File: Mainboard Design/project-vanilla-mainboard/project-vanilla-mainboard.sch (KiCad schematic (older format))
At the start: 5 parts

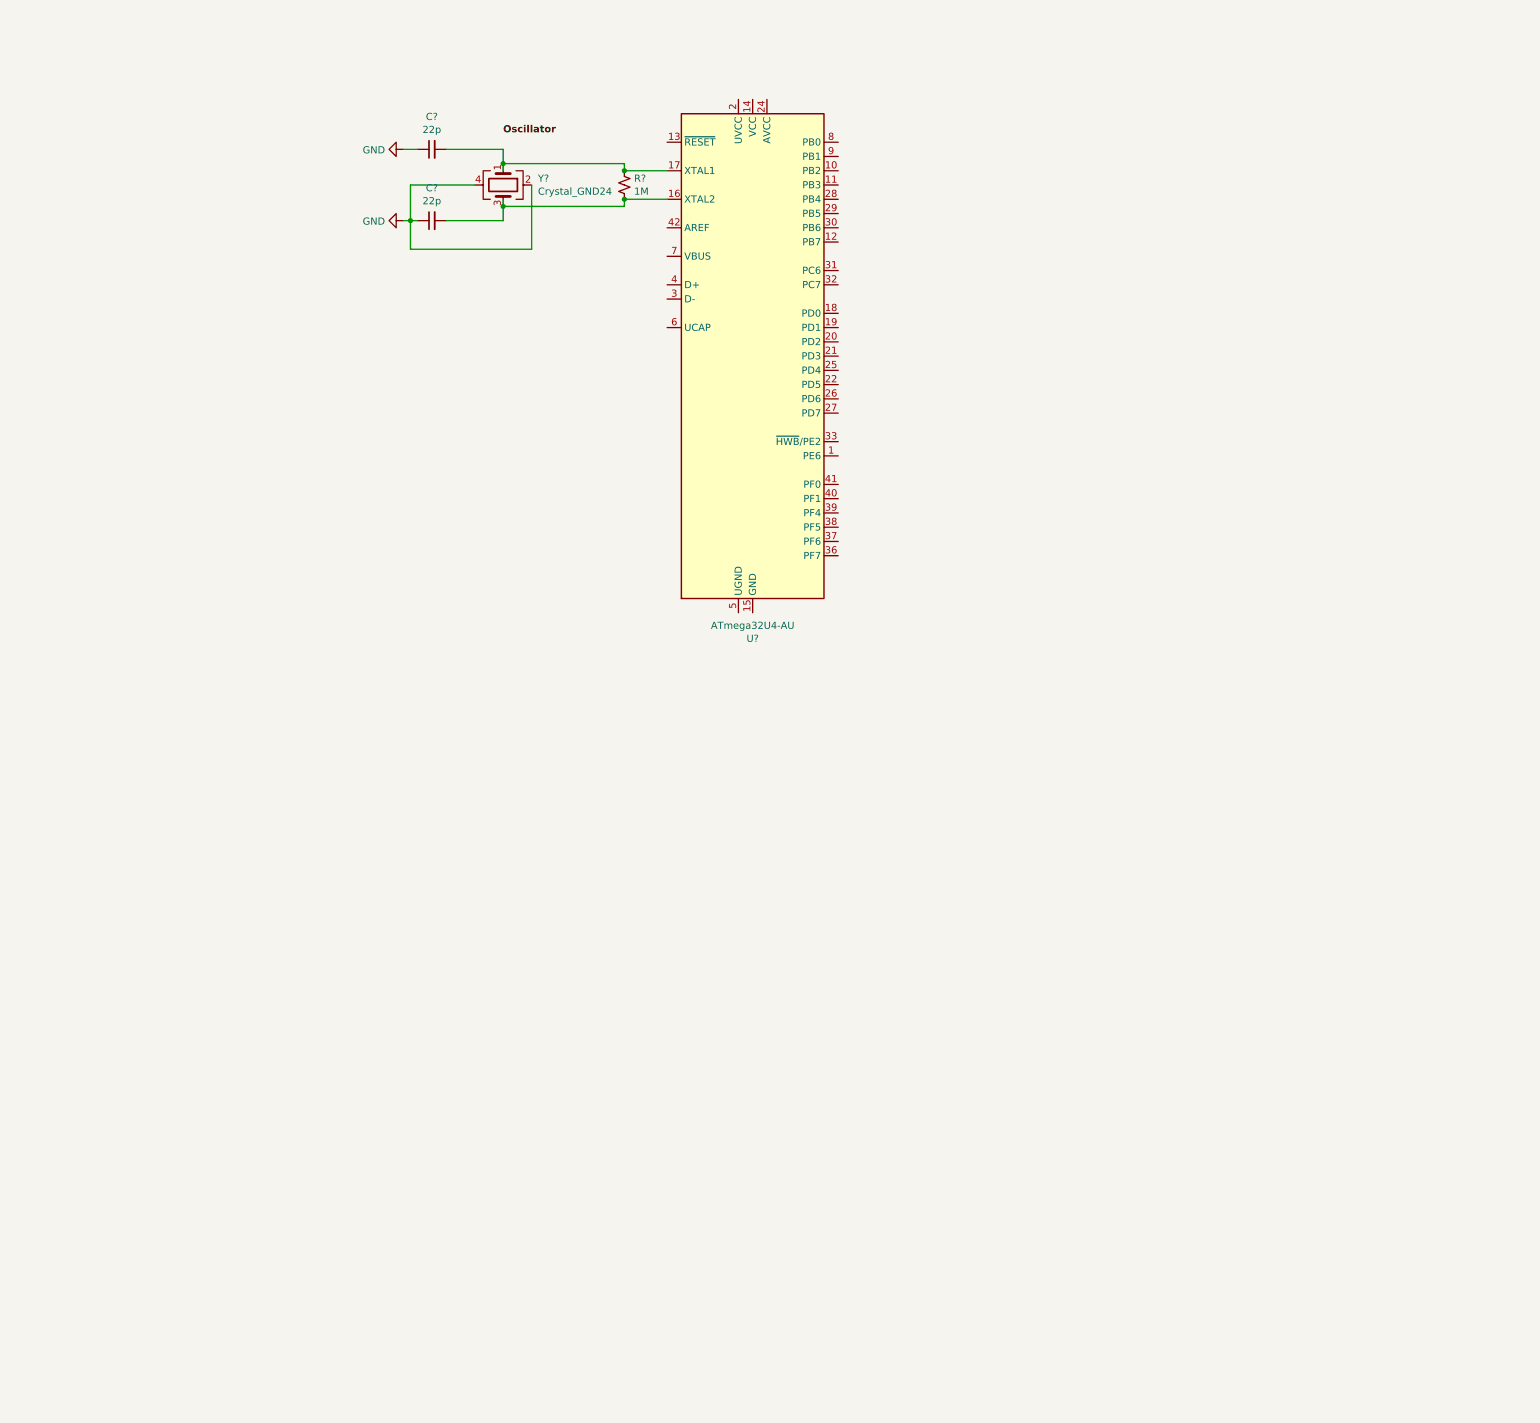
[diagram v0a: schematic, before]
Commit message: Major changes to both case design and mainboard schematic. Nothing final yet.
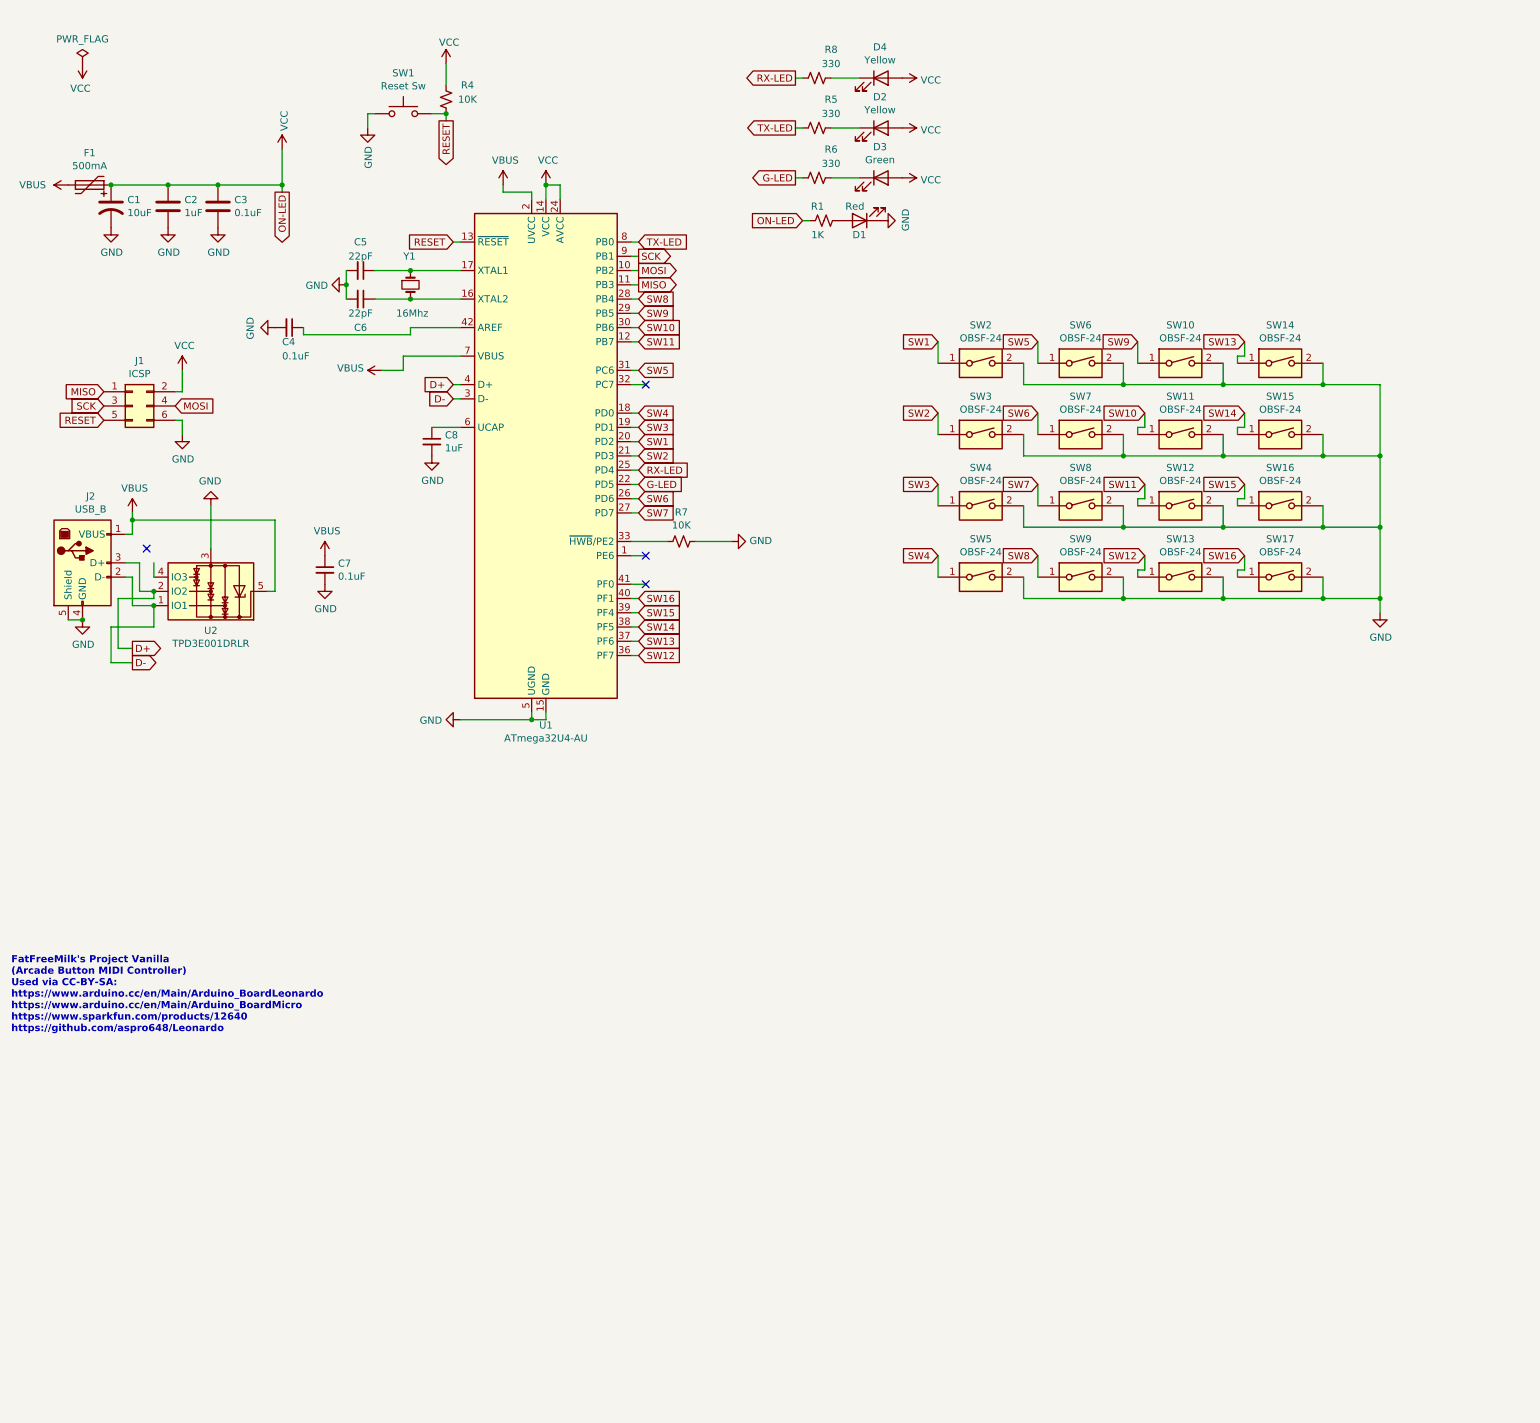
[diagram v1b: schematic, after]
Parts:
- removed C? (x2): 22p, symbol Device:C_Small
- removed R?: 1M, symbol Device:R_Small_US
- removed U?: ATmega32U4-AU, Package_QFP:TQFP-44_10x10mm_P0.8mm, symbol MCU_Microchip_ATmega:ATmega32U4-AU
- removed Y?: Crystal_GND24, symbol Device:Crystal_GND24
- added C1: 10uF, symbol Device:CP1
- added C2: 1uF, symbol Device:C
- added C3: 0.1uF, symbol Device:C
- added C4, C7: 0.1uF, symbol Device:C_Small
- added C5, C6: 22pF, symbol Device:C_Small
- added C8: 1uF, symbol Device:C_Small
- added D1: Red, symbol Device:LED
- added D2, D4: Yellow, symbol Device:LED
- added D3: Green, symbol Device:LED
- added F1: 500mA, symbol Device:Polyfuse
- added J1: ICSP, symbol Connector_Generic:Conn_02x03_Odd_Even
- added J2: USB_B, symbol Connector:USB_B
- added R1: 1K, symbol Device:R_Small_US
- added R4, R7: 10K, symbol Device:R_Small_US
- added R5, R6, R8: 330, symbol Device:R_Small_US
- added SW1: Reset Sw, symbol Switch:SW_MEC_5G
- added SW10, SW11, SW12, SW13, SW14, SW15, SW16, SW17, SW2, SW3, SW4, SW5, SW6, SW7, SW8, SW9: OBSF-24, symbol Switch:SW_DIP_x01
- added U1: ATmega32U4-AU, Package_QFP:TQFP-44_10x10mm_P0.8mm, symbol MCU_Microchip_ATmega:ATmega32U4-AU
- added U2: TPD3E001DRLR, Package_TO_SOT_SMD:SOT-553, symbol Power_Protection:TPD3E001DRLR
- added Y1: 16Mhz, symbol Device:Crystal_Small
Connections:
- net labels added: D+, D-, G-LED, MISO, MOSI, ON-LED, RESET, RX-LED, SCK, SW1, SW10, SW11, SW12, SW13, SW14, SW15, SW16, SW2, SW3, SW4, SW5, SW6, SW7, SW8, SW9, TX-LED, VBUS, VCC
- net labels removed: Oscillator
- wire segments 20 -> 164
- no-connect marks 0 -> 4
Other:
- note added: "FatFreeMilk's Project Vanilla\n(Arcade Button MIDI Controller)\nUsed via CC-BY-SA:\nhttps://www.arduino.cc/en/Main/Arduino_BoardLeonardo\nhttps://www.arduino.cc/en/Main/Arduino_BoardMicro\nhttps://www.sparkfun.com/products/12640\nhttps://github.com/aspro648/Leonardo"

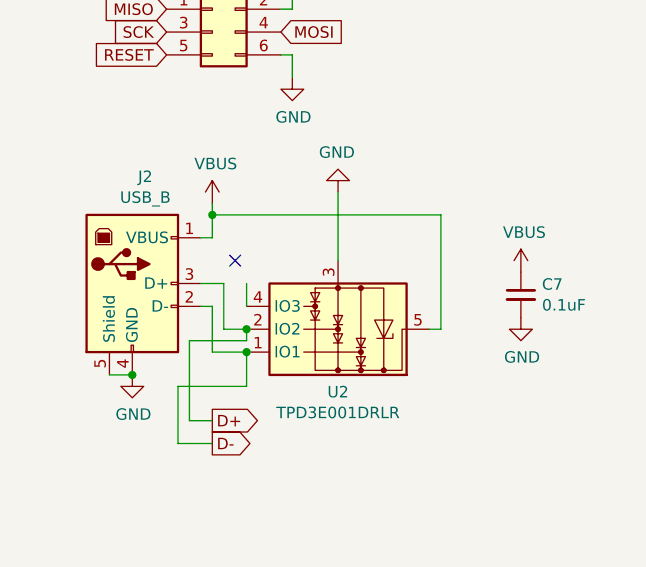
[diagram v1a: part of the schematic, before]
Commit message: Started work on the case in FreeCAD (new design).
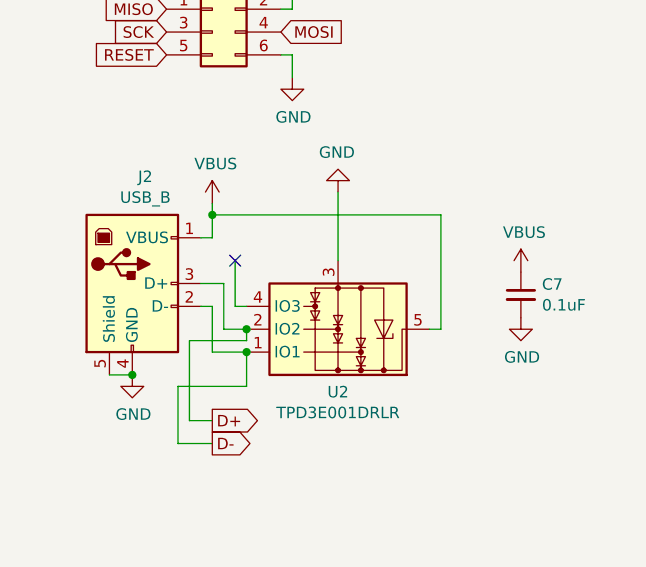
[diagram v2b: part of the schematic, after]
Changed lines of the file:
@@
 Wire Wire Line
 	1950 4000 1950 4300
-NoConn ~ 1500 4300
-Wire Wire Line
-	1550 4400 1550 4500
 Wire Wire Line
 	3600 1250 3600 1300
@@
 Wire Wire Line
 	3650 2150 3700 2150
+NoConn ~ 1500 4300
+Wire Wire Line
+	1550 4500 1500 4500
+Wire Wire Line
+	1500 4500 1500 4300
 $EndSCHEMATC

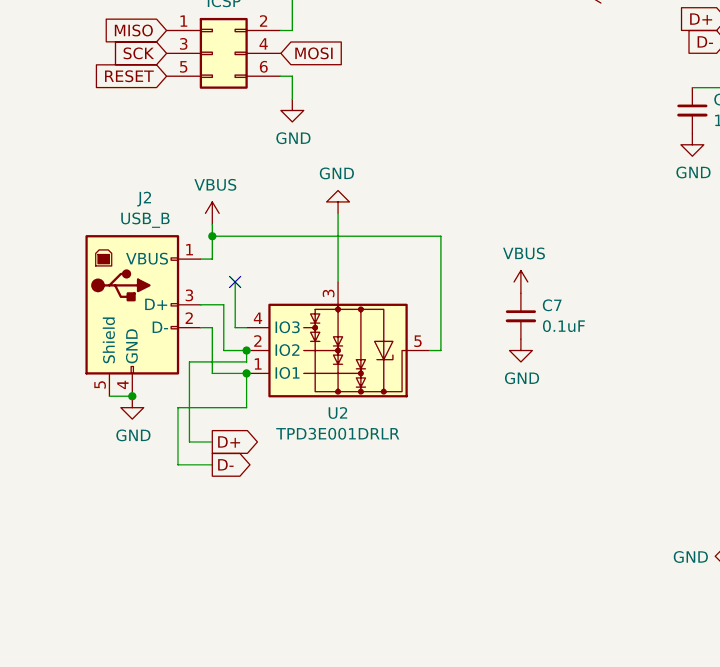
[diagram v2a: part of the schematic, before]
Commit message: In the middle of updating schematic and finishing shell design.
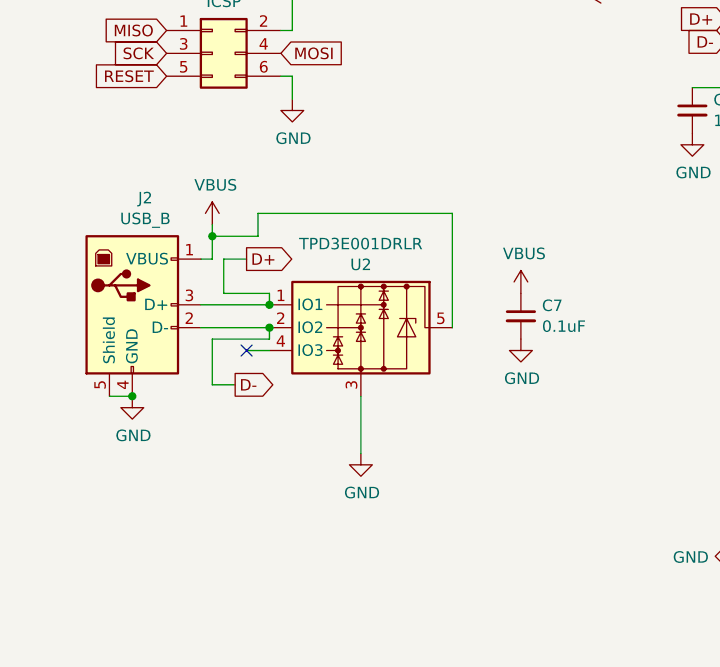
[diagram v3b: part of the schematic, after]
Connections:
- net D+: now also U2.1 (IO1); no longer U2.2 (IO2)
- net D-: now also U2.2 (IO2); no longer U2.1 (IO1)
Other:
- moved on the sheet: U2
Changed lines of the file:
@@
-$EndComp
-$Comp
-L Connector:USB_B J2
-U 1 1 5FF3196E
-P 1050 4400
-F 0 "J2" H 1107 4867 50  0000 C CNN
-F 1 "USB_B" H 1107 4776 50  0000 C CNN
-F 2 "" H 1200 4350 50  0001 C CNN
-F 3 " ~" H 1200 4350 50  0001 C CNN
-	1    1050 4400
-	1    0    0    -1
 $EndComp
 $Comp
@@
 Wire Wire Line
 	950  4800 1050 4800
-Connection ~ 1050 4800
-Wire Wire Line
-	1400 4050 1400 4100
 Wire Wire Line
 	1400 4200 1350 4200
@@
 L Power_Protection:TPD3E001DRLR U2
 U 1 1 60054A8D
-P 1950 4600
-F 0 "U2" H 1950 4875 50  0000 C CNN
-F 1 "TPD3E001DRLR" H 1950 4966 50  0000 C CNN
-F 2 "Package_TO_SOT_SMD:SOT-553" H 1250 4300 50  0001 C CNN
-F 3 "http://www.ti.com/lit/ds/symlink/tpd3e001.pdf" H 1750 4850 50  0001 C CNN
-	1    1950 4600
-	-1   0    0    1
-$EndComp
-Wire Wire Line
-	1400 4100 2400 4100
-Connection ~ 1400 4100
-Wire Wire Line
-	1400 4100 1400 4200
-Wire Wire Line
-	2400 4600 2350 4600
-Wire Wire Line
-	2400 4100 2400 4600
-Wire Wire Line
-	1350 4500 1400 4500
-Wire Wire Line
-	1400 4500 1400 4700
-Wire Wire Line
-	1400 4700 1550 4700
-Wire Wire Line
-	1350 4400 1450 4400
-Wire Wire Line
-	1450 4400 1450 4600
-Wire Wire Line
-	1450 4600 1550 4600
-Text GLabel 1400 5000 2    50   Output ~ 0
-D+
-Text GLabel 1400 5100 2    50   Output ~ 0
-D-
-Wire Wire Line
-	1550 4700 1550 4850
-Wire Wire Line
-	1550 4850 1250 4850
-Wire Wire Line
-	1250 4850 1250 5100
-Wire Wire Line
-	1250 5100 1400 5100
-Connection ~ 1550 4700
-Wire Wire Line
-	1550 4600 1550 4650
-Wire Wire Line
-	1550 4650 1300 4650
-Wire Wire Line
-	1300 4650 1300 5000
-Wire Wire Line
-	1300 5000 1400 5000
-Connection ~ 1550 4600
+P 2050 4500
+F 0 "U2" H 2050 4775 50  0000 C CNN
+F 1 "TPD3E001DRLR" H 2050 4866 50  0000 C CNN
+F 2 "Package_TO_SOT_SMD:SOT-553" H 1350 4200 50  0001 C CNN
+F 3 "http://www.ti.com/lit/ds/symlink/tpd3e001.pdf" H 1850 4750 50  0001 C CNN
+	1    2050 4500
+	-1   0    0    -1
+$EndComp
 Text GLabel 3650 3150 0    50   Input ~ 0
 D+
@@
 L power:GND #PWR0128
 U 1 1 60167591
-P 1950 4000
-F 0 "#PWR0128" H 1950 3750 50  0001 C CNN
-F 1 "GND" H 1955 3827 50  0000 C CNN
-F 2 "" H 1950 4000 50  0001 C CNN
-F 3 "" H 1950 4000 50  0001 C CNN
-	1    1950 4000
-	-1   0    0    1
-$EndComp
-Wire Wire Line
-	1950 4000 1950 4300
+P 2050 5050
+F 0 "#PWR0128" H 2050 4800 50  0001 C CNN
+F 1 "GND" H 2055 4877 50  0000 C CNN
+F 2 "" H 2050 5050 50  0001 C CNN
+F 3 "" H 2050 5050 50  0001 C CNN
+	1    2050 5050
+	1    0    0    -1
+$EndComp
 Wire Wire Line
 	3600 1250 3600 1300
@@
 Wire Wire Line
 	3650 2150 3700 2150
-NoConn ~ 1500 4300
-Wire Wire Line
-	1550 4500 1500 4500
-Wire Wire Line
-	1500 4500 1500 4300
+Connection ~ 1050 4800
+$Comp
+L Connector:USB_B J2
+U 1 1 5FF3196E
+P 1050 4400
+F 0 "J2" H 1107 4867 50  0000 C CNN
+F 1 "USB_B" H 1107 4776 50  0000 C CNN
+F 2 "" H 1200 4350 50  0001 C CNN
+F 3 " ~" H 1200 4350 50  0001 C CNN
+	1    1050 4400
+	1    0    0    -1
+$EndComp
+Wire Wire Line
+	1400 4050 1400 4100
+Wire Wire Line
+	1350 4400 1650 4400
+Wire Wire Line
+	1350 4500 1650 4500
+Wire Wire Line
+	1650 4600 1550 4600
+NoConn ~ 1550 4600
+Wire Wire Line
+	1400 4100 1600 4100
+Wire Wire Line
+	1600 4100 1600 4000
+Wire Wire Line
+	1600 4000 2450 4000
+Wire Wire Line
+	2450 4000 2450 4500
+Connection ~ 1400 4100
+Wire Wire Line
+	1400 4100 1400 4200
+Wire Wire Line
+	2050 4800 2050 5050
+Wire Wire Line
+	1650 4400 1650 4350
+Wire Wire Line
+	1650 4350 1450 4350
+Connection ~ 1650 4400
+Wire Wire Line
+	1650 4500 1650 4550
+Wire Wire Line
+	1650 4550 1400 4550
+Wire Wire Line
+	1400 4550 1400 4750
+Wire Wire Line
+	1400 4750 1500 4750
+Connection ~ 1650 4500
+Wire Wire Line
+	1450 4350 1450 4200
+Wire Wire Line
+	1450 4200 1550 4200
+Text GLabel 1550 4200 2    50   Output ~ 0
+D+
+Text GLabel 1500 4750 2    50   Output ~ 0
+D-
 $EndSCHEMATC

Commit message: Major updates to schematic.
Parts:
- removed F1: 500mA, symbol Device:Polyfuse
- removed SW1: Reset Sw, symbol Switch:SW_MEC_5G
- removed SW17: OBSF-24, symbol Switch:SW_DIP_x01
- removed U2: TPD3E001DRLR, Package_TO_SOT_SMD:SOT-553, symbol Power_Protection:TPD3E001DRLR
- added C9: 150uF, symbol Device:C_Small
- added D10, D11, D12, D13, D14, D15, D16, D17, D18, D19, D20, D5, D6, D7, D8, D9: 1N4148WS, Diode_SMD:D_SOD-323, symbol Diode:1N4148WS
- added R10, R2, R3, R9: 10K, symbol Device:R_Small_US
- added SW2: OBSF-24, symbol Switch:SW_DIP_x01
- added U2: TPD3S014, Package_TO_SOT_SMD:SOT-23-6, symbol Power_Protection:TPD3S014
- C7: value 0.1uF -> 1uF
- renumbered SW2 to SW1
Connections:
- net VCC is gone; now on net VBUS: C1.1, C2.1, C3.1, D2.2 (A), D3.2 (A), D4.2 (A), J1.2 (Pin_2), R1.1, R4.2, U1.14 (VCC), U1.24 (AVCC), U1.34 (VCC), U1.44 (AVCC)
- net D+: now also U2.6 (D2)
- net D-: now also U2.5 (D1)
- net GND: now also C9.1, U2.2 (GND); no longer SW1.2, SW10.2, SW11.2, SW12.2, SW13.2, SW14.2, SW15.2, SW16.2, SW3.2, SW4.2, SW5.2, SW6.2, SW7.2, SW8.2, SW9.2
- net SW10: no longer SW11.1
- net SW11: no longer SW12.1
- net SW12: no longer SW13.1
- net SW13: no longer SW14.1
- net SW14: no longer SW15.1
- net SW15: no longer SW16.1
- net SW9: no longer SW10.1
- net VBUS: now also R10.1, R2.1, R3.1, R9.1, U2.4 (OUT); no longer J2.1 (VBUS)
- net SW1: no longer names the net of SW1.1
- net SW1: now also D5.2 (A); no longer U1.20 (PD2)
- net SW2: no longer names the net of SW3.1
- net SW2: now also D7.2 (A); no longer U1.21 (PD3)
- net SW3: no longer names the net of SW4.1
- net SW3: now also D8.2 (A); no longer U1.19 (PD1)
- net SW4: no longer names the net of SW5.1
- net SW4: now also D9.2 (A); no longer U1.18 (PD0)
- net SW5: no longer names the net of SW6.1
- net SW5: now also D10.2 (A); no longer U1.31 (PC6)
- net SW6: no longer names the net of SW7.1
- net SW6: now also D11.2 (A); no longer U1.26 (PD6)
- net SW7: no longer names the net of SW8.1
- net SW7: now also D12.2 (A); no longer U1.27 (PD7)
- net SW8: no longer names the net of SW9.1
- net SW8: now also D13.2 (A); no longer U1.28 (PB4)
- new net: D17.2 (A), SW13.1
- new net: D6.2 (A), SW2.1
- new net: D14.2 (A), SW10.1
- new net: D18.2 (A), SW14.1
- new net: D15.2 (A), SW11.1
- new net: D19.2 (A), SW15.1
- new net: D16.2 (A), SW12.1
- new net: D20.2 (A), SW16.1
- new net COL1: R2.2, SW1.2, SW2.2, SW3.2, SW4.2, U1.31 (PC6)
- new net COL2: R3.2, SW5.2, SW6.2, SW7.2, SW8.2, U1.26 (PD6)
- new net COL3: R9.2, SW10.2, SW11.2, SW12.2, SW9.2, U1.27 (PD7)
- new net COL4: R10.2, SW13.2, SW14.2, SW15.2, SW16.2, U1.28 (PB4)
- new net R1: D13.1 (K), D17.1 (K), D5.1 (K), D9.1 (K), U1.20 (PD2)
- new net R2: D10.1 (K), D14.1 (K), D18.1 (K), D6.1 (K), U1.21 (PD3)
- new net R3: D11.1 (K), D15.1 (K), D19.1 (K), D7.1 (K), U1.19 (PD1)
- new net R4: D12.1 (K), D16.1 (K), D20.1 (K), D8.1 (K), U1.18 (PD0)
- new net V-IN: C9.2, J2.1 (VBUS), U2.3 (IN)
- no-connect marks 4 -> 12
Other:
- moved on the sheet: C7, D1, D2, D3, D4, R1, R4, R5, R6, R8, SW1
